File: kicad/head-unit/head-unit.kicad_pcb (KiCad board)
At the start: 4 copper layers, 59 parts, among them J1 Debug_Port, J2 Relay_Main_Power, J3 Steering_Wheel, J4 Power Port, J5 Car Connection, J6 Relay_Ign_Detect, J7 Pi, J8 DAC+, K1 Relay_Aux_Power, K2 Relay_Amplifier, SW1 SW_RST, U1 ADP1108AN-3.3, U2 STM32F401RCTx, U3 ADP1108AN-5

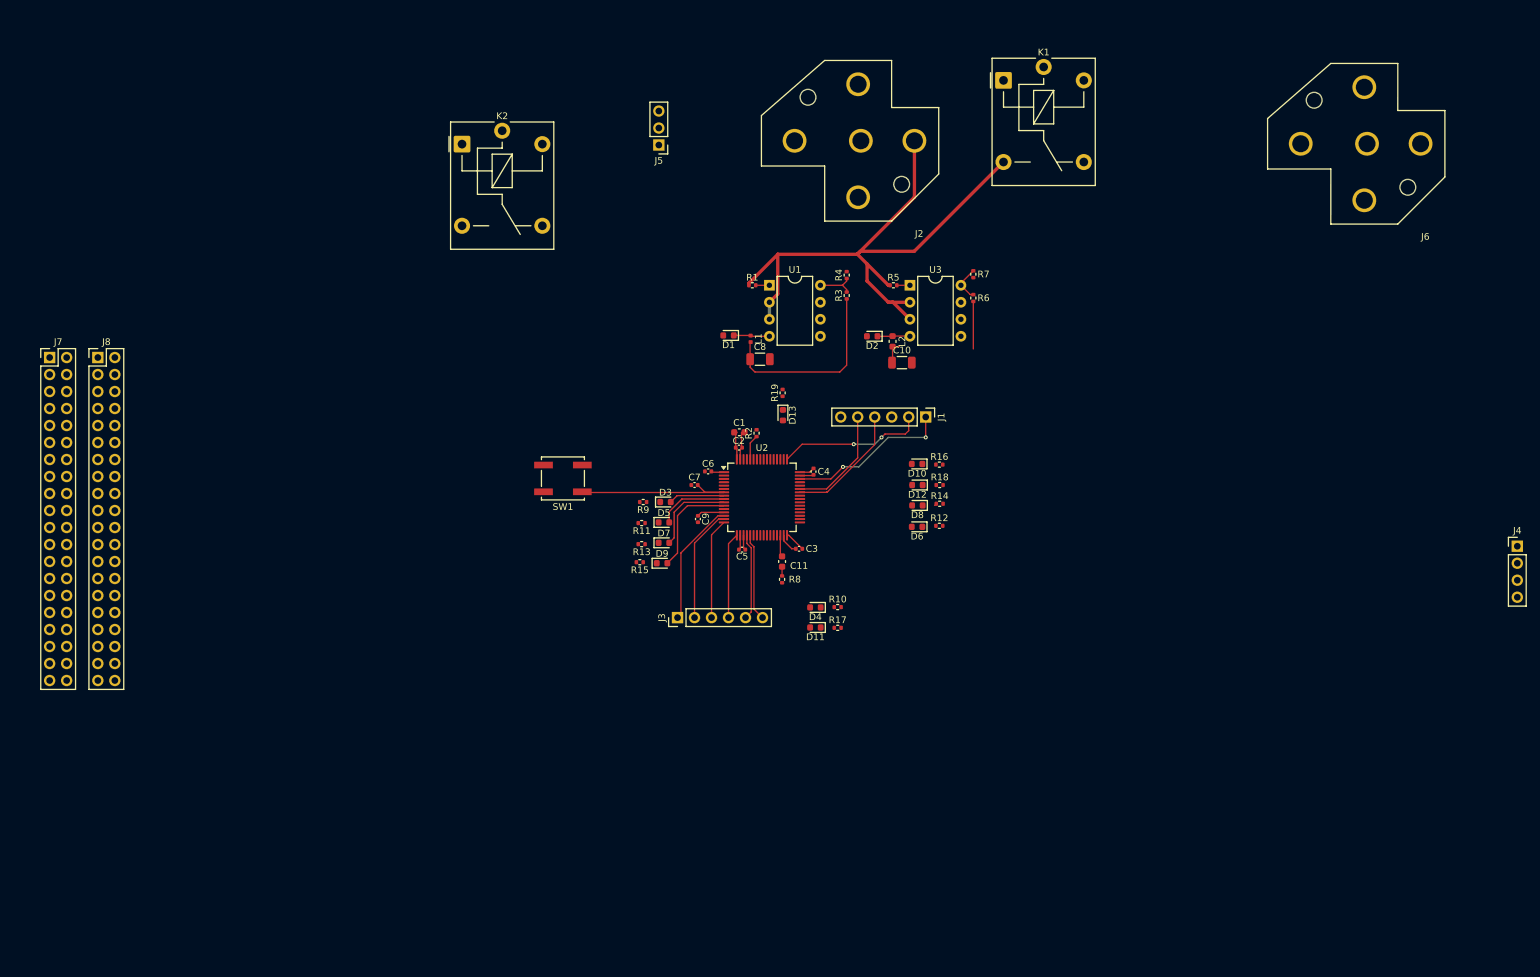
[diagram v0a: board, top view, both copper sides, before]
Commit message: Fix mosfets, switch to screw terminals and XT60
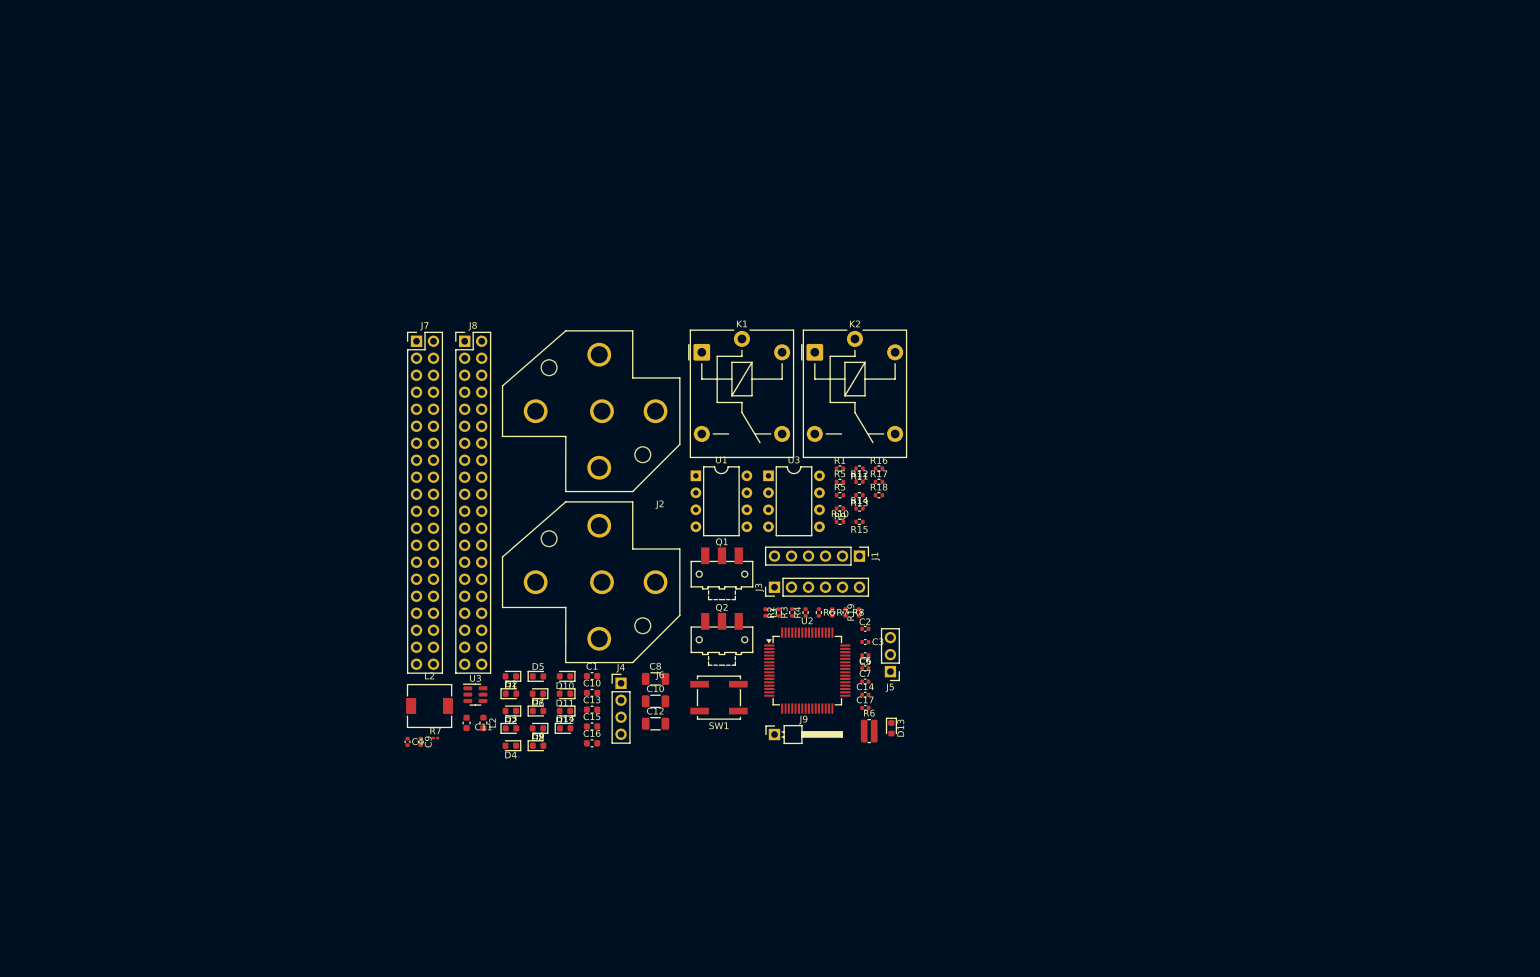
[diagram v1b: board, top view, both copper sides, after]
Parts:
- added C10: 10uF, Capacitor_SMD:C_0603_1608Metric, F.Cu at (133.5, 112.3)
- added C12: 100uF, Capacitor_SMD:C_1206_3216Metric, F.Cu at (143.0, 117.0)
- added C13: 22uF, Capacitor_SMD:C_0603_1608Metric, F.Cu at (133.5, 114.8)
- added C14: 100nF, Capacitor_SMD:C_0402_1005Metric, F.Cu at (174.4, 112.6)
- added C15: 22uF, Capacitor_SMD:C_0603_1608Metric, F.Cu at (133.5, 117.4)
- added C16: 10uF, Capacitor_SMD:C_0603_1608Metric, F.Cu at (133.5, 119.9)
- added C17: 100nF, Capacitor_SMD:C_0402_1005Metric, F.Cu at (174.4, 114.6)
- added D14: D_Schottky, Diode_SMD:D_0603_1608Metric, F.Cu at (129.5, 117.6)
- added D2: D_Schottky, Diode_SMD:D_0603_1608Metric, F.Cu at (121.4, 112.5)
- added J9: Amp_Remote, Connector_PinHeader_2.54mm:PinHeader_1x01_P2.54mm_Horizontal, F.Cu at (160.8, 118.6)
- added L2: 5.6uH, Inductor_SMD:L_6.3x6.3_H3, F.Cu at (109.3, 114.3)
- added Q1: NMOS, Button_Switch_SMD:SW_SPDT_CK-JS102011SAQN, F.Cu at (152.9, 94.6)
- added Q2: NMOS, Button_Switch_SMD:SW_SPDT_CK-JS102011SAQN, F.Cu at (152.9, 104.4)
- added R5: 10K, Resistor_SMD:R_0402_1005Metric, F.Cu at (170.6, 80.8)
- added R6: 102K2, Resistor_SMD:R_0612_1632Metric, F.Cu at (174.9, 118.0)
- added R7: 30R, Resistor_SMD:R_0201_0603Metric, F.Cu at (110.1, 119.1)
- added U3: TPS56339DDC, Package_TO_SOT_SMD:SOT-23-6, F.Cu at (116.1, 112.6)
- R3: value 456K -> 9K
- R4: value 33K -> 3K3
- moved J4 135.5 mm to (137.9, 110.9)
- moved J6 131.8 mm to (134.6, 95.8)
- moved J5 86.0 mm to (178.1, 109.2)
- moved L2 83.6 mm to (117.3, 116.8)
- moved D2 77.8 mm to (121.4, 115.0)
- moved C4 72.9 mm to (106.0, 119.7)
- moved D8 65.8 mm to (125.4, 117.6)
- moved C10 62.6 mm to (143.0, 113.6)
- moved D12 62.6 mm to (129.5, 115.0)
- moved D6 61.9 mm to (125.4, 112.5)
- moved D10 61.4 mm to (129.5, 109.9)
- moved K2 61.2 mm to (166.8, 61.5)
- moved K1 60.7 mm to (149.9, 61.5)
- moved D1 60.4 mm to (121.4, 109.9)
- moved J2 55.9 mm to (134.6, 70.3)
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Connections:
- J2 pad 87: Net-(U1-SW1) -> +12V_Switched
- K1 pad 14: Net-(U1-SW1) -> +12V_Switched
- K1 pad A1: GND -> Net-(Q1-S)
- K1 pad A2: Aux_Power -> +5V
- K2 pad 14: Amp_Remote -> Net-(J9-Pin_1)
- K2 pad A1: GND -> Net-(Q2-S)
- K2 pad A2: Amp_Remote_3V3 -> +5V
- R1 pad 1: Net-(U1-SW1) -> +12V_Switched
- U1 pad 2: Net-(U1-SW1) -> +12V_Switched
- U1 pad 3: Net-(U1-SW1) -> +12V_Switched
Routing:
- net Net-(U1-SW1): track 97.9 -> 0.00 mm
- net +3V3: track 40.7 -> 0.00 mm
- net Net-(U2-NRST): track 25.6 -> 0.00 mm
- net SWDIO: track 24.4 -> 0.00 mm, vias 2 -> 0
- net SWCLK: track 22.0 -> 0.00 mm, vias 2 -> 0
- net Steering_Yellow: track 18.6 -> 0.00 mm
- net USART_Debug_TX: track 18.2 -> 0.00 mm
- net Steering_Green: track 17.0 -> 0.00 mm
- net USART_Debug_RX: track 16.7 -> 0.00 mm
- net AA_TrackNext_LED: track 15.3 -> 0.00 mm
- net Steering_Blue: track 15.0 -> 0.00 mm
- net Steering_Brown: track 13.1 -> 0.00 mm
- net AA_VolDown_LED: track 12.9 -> 0.00 mm
- net Steering_Black: track 12.9 -> 0.00 mm
- net Steering_Red: track 12.8 -> 0.00 mm
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
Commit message: Add I2C, begin routing
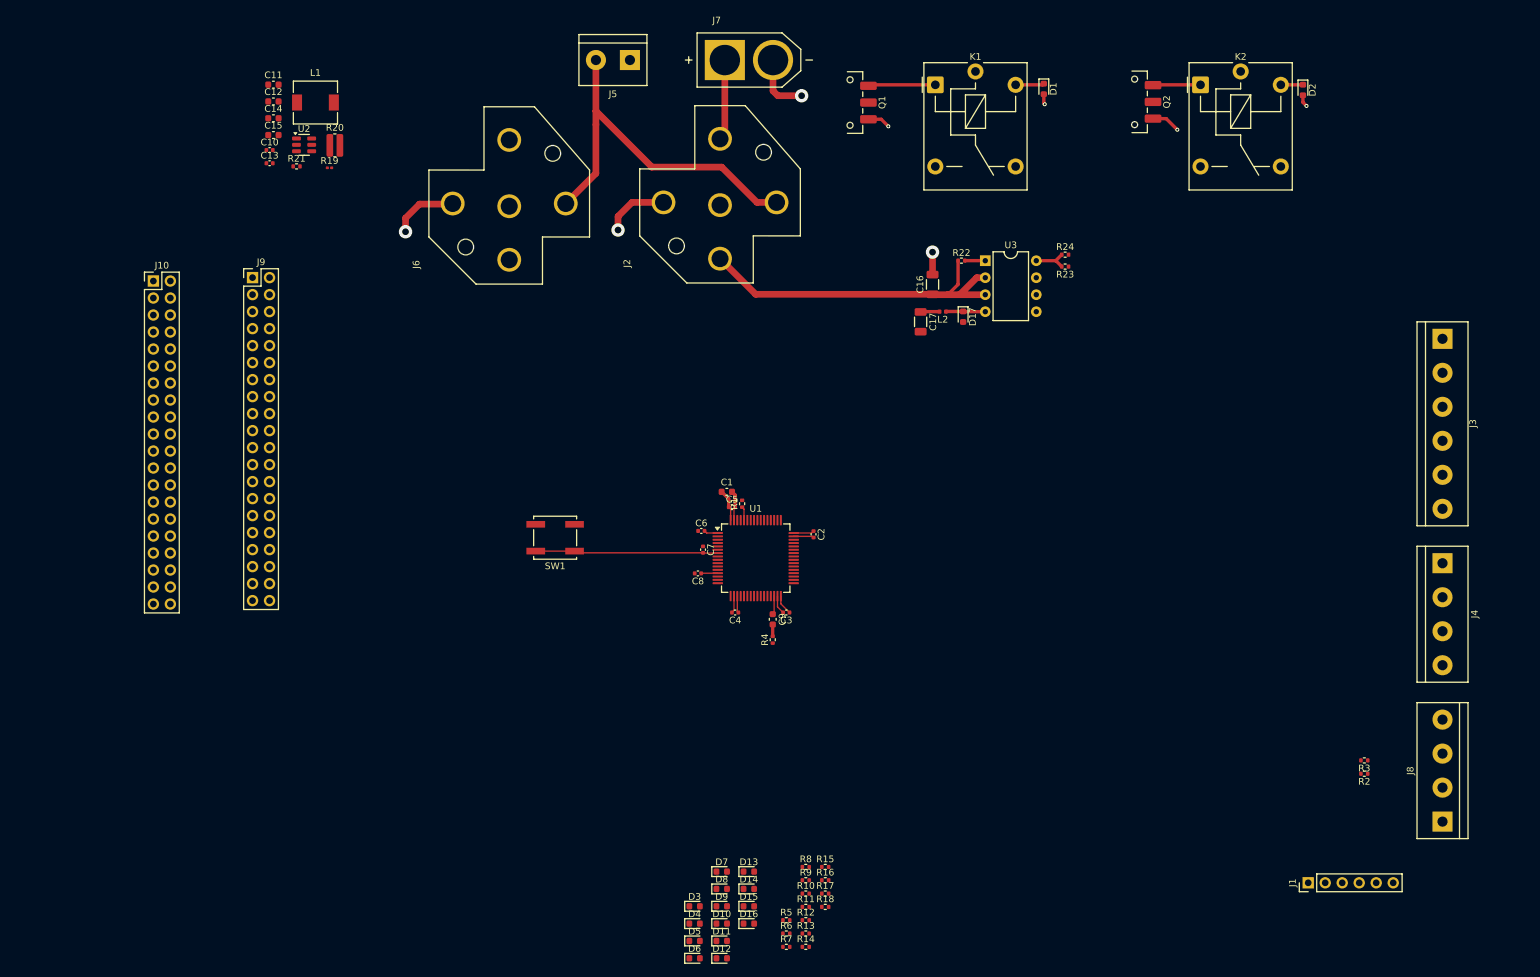
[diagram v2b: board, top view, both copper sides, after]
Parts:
- removed the C10 at (143.0, 113.6)
- removed the C10 at (133.5, 112.3)
- removed the D2 at (121.4, 115.0)
- removed the D2 at (121.4, 112.5)
- removed the L2 at (109.3, 114.3)
- removed the L2 at (117.3, 116.8)
- removed the R5 at (170.6, 82.8)
- removed the R5 at (170.6, 80.8)
- removed the R6 at (174.9, 118.0)
- removed the R6 at (167.4, 100.3)
- removed the R7 at (169.4, 100.3)
- removed the R7 at (110.1, 119.1)
- removed the U3 at (116.1, 112.6)
- removed the U3 at (159.9, 79.9)
- added C10: 100nF, Capacitor_SMD:C_0402_1005Metric, F.Cu at (85.4, 31.2)
- added D15: LED, LED_SMD:LED_0603_1608Metric, F.Cu at (157.0, 144.2)
- added D16: LED, LED_SMD:LED_0603_1608Metric, F.Cu at (157.0, 146.8)
- added D17: D_Schottky, Diode_SMD:D_0603_1608Metric, F.Cu at (189.0, 56.1)
- added D2: D_Schottky, Diode_SMD:D_0603_1608Metric, F.Cu at (239.7, 22.3)
- added J10: DAC+, Connector_PinHeader_2.54mm:PinHeader_2x20_P2.54mm_Vertical, F.Cu at (68.0, 50.8)
- added L2: 1uH, Inductor_SMD:L_0402_1005Metric, F.Cu at (185.9, 55.4)
- added R20: 102K2, Resistor_SMD:R_0612_1632Metric, F.Cu at (95.1, 30.5)
- added R21: 10K, Resistor_SMD:R_0402_1005Metric, F.Cu at (89.4, 33.7)
- added R22: 100R, Resistor_SMD:R_0402_1005Metric, F.Cu at (188.7, 47.8)
- added R23: 9K, Resistor_SMD:R_0402_1005Metric, F.Cu at (204.2, 48.6)
- added R24: 3K3, Resistor_SMD:R_0402_1005Metric, F.Cu at (204.2, 46.9)
- added R5: 2K2, Resistor_SMD:R_0402_1005Metric, F.Cu at (162.6, 146.3)
- added R6: 2K2, Resistor_SMD:R_0402_1005Metric, F.Cu at (162.6, 148.3)
- added R7: 2K2, Resistor_SMD:R_0402_1005Metric, F.Cu at (162.6, 150.3)
- added U3: ADP1108AN-3.3, Package_DIP:DIP-8_W7.62mm, F.Cu at (192.3, 47.8)
- C11: value 5uF -> 10uF
- C12: value 100uF -> 10uF; footprint Capacitor_SMD:C_1206_3216Metric -> Capacitor_SMD:C_0603_1608Metric
- C13: value 22uF -> 100nF; footprint Capacitor_SMD:C_0603_1608Metric -> Capacitor_SMD:C_0402_1005Metric
- C14: value 100nF -> 22uF; footprint Capacitor_SMD:C_0402_1005Metric -> Capacitor_SMD:C_0603_1608Metric
- C16: value 10uF -> 100uF; footprint Capacitor_SMD:C_0603_1608Metric -> Capacitor_SMD:C_1206_3216Metric
- C17: value 100nF -> 100uF; footprint Capacitor_SMD:C_0402_1005Metric -> Capacitor_SMD:C_1206_3216Metric
- C8: value 100uF -> 1 uF; footprint Capacitor_SMD:C_1206_3216Metric -> Capacitor_SMD:C_0402_1005Metric
- C9: value 1 uF -> 5uF; footprint Capacitor_SMD:C_0402_1005Metric -> Capacitor_SMD:C_0603_1608Metric
- D14: value D_Schottky -> LED; footprint Diode_SMD:D_0603_1608Metric -> LED_SMD:LED_0603_1608Metric
- J2, J6: footprint external_symbols:TE_VCF4-1000 -> vcf4:TE_VCF4-1000
- J3: footprint Connector_PinHeader_2.54mm:PinHeader_1x06_P2.54mm_Vertical -> TerminalBlock:TerminalBlock_bornier-6_P5.08mm
- J4: value Power Port -> Power_Port; footprint Connector_PinHeader_2.54mm:PinHeader_1x04_P2.54mm_Vertical -> TerminalBlock:TerminalBlock_bornier-4_P5.08mm
- J5: value Car Connection -> Remote; footprint Connector_PinHeader_2.54mm:PinHeader_1x03_P2.54mm_Vertical -> TerminalBlock:TerminalBlock_bornier-2_P5.08mm
- J7: value Pi -> XT60-M; footprint Connector_PinHeader_2.54mm:PinHeader_2x20_P2.54mm_Vertical -> xt60:AMASS_XT60-M
- J8: value DAC+ -> I2C_Interface; footprint Connector_PinHeader_2.54mm:PinHeader_2x20_P2.54mm_Vertical -> TerminalBlock:TerminalBlock_bornier-4_P5.08mm
- J9: value Amp_Remote -> Pi; footprint Connector_PinHeader_2.54mm:PinHeader_1x01_P2.54mm_Horizontal -> Connector_PinHeader_2.54mm:PinHeader_2x20_P2.54mm_Vertical
- L1: value 1uH -> 5.6uH; footprint Inductor_SMD:L_0402_1005Metric -> Inductor_SMD:L_6.3x6.3_H3
- Q1, Q2: footprint Button_Switch_SMD:SW_SPDT_CK-JS102011SAQN -> Button_Switch_SMD:SW_SPDT_CK_JS102011SAQN
- R1: value 100R -> 10K
- R19: value 2K2 -> 30R; footprint Resistor_SMD:R_0402_1005Metric -> Resistor_SMD:R_0201_0603Metric
- R2: value 10K -> 2K7
- R3: value 9K -> 2K7
- R4: value 3K3 -> 1R
- R8: value 1R -> 2K2
- U1: value ADP1108AN-3.3 -> STM32F401RCTx; footprint Package_DIP:DIP-8_W7.62mm -> Package_QFP:LQFP-64_10x10mm_P0.5mm
- U2: value STM32F401RCTx -> TPS56339DDC; footprint Package_QFP:LQFP-64_10x10mm_P0.5mm -> Package_TO_SOT_SMD:SOT-23-6
- moved J8 162.8 mm to (260.6, 131.6), turned to 90 degrees
- moved J4 124.0 mm to (260.6, 93.0), turned to -90 degrees
- moved C14 123.5 mm to (85.9, 26.5)
- moved D1 118.5 mm to (201.0, 22.1), turned to -90 degrees
- moved C12 109.1 mm to (85.9, 24.0)
- moved U2 108.7 mm to (90.5, 30.5)
- moved J3 106.5 mm to (260.6, 59.4), turned to -90 degrees
- moved J9 103.6 mm to (82.8, 50.3)
- moved R19 103.3 mm to (94.3, 33.9), turned to 0 degrees
- moved L1 101.6 mm to (92.2, 24.1), turned to 0 degrees
- moved Q2 101.3 mm to (214.6, 24.0), turned to -90 degrees
- moved C15 100.4 mm to (85.9, 29.0)
- moved C11 99.6 mm to (85.9, 21.5), turned to 0 degrees
- moved J5 99.3 mm to (139.2, 17.8)
- moved C13 94.8 mm to (85.4, 33.2)
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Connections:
- C11 pad 1: Net-(U2-VCAP1) -> +12V_Switched
- C11 pad 2: Net-(C11-Pad2) -> GND
- C13 pad 1: +5V -> +12V_Switched
- C14 pad 1: Net-(C14-Pad1) -> +5V
- C14 pad 2: Net-(U3-SW) -> GND
- C17 pad 1: +12V_Switched -> +3V3
- C6 pad 2: Net-(U2-VBAT) -> Net-(U1-VBAT)
- C7 pad 2: Net-(U2-NRST) -> Net-(U1-NRST)
- C8 pad 1: +3V3 -> Net-(U1-VREF+)
- C8 pad 2: GND -> +3V3
- C9 pad 1: Net-(U2-VREF+) -> Net-(U1-VCAP1)
- C9 pad 2: +3V3 -> Net-(C9-Pad2)
- D1 pad 1: Net-(D1-K) -> +5V
- D14 pad 1: +5V -> Net-(D14-K)
- D14 pad 2: GND -> Power_LED
- J4 pad 1: GND -> +3V3
- J4 pad 2: +3V3 -> +5V
- J4 pad 3: +5V -> +12V
- J4 pad 4: +12V -> GND
- J5 pad 1: +12V -> Amp_Remote
- J5 pad 2: GND -> Car_Remote
- J8 pad 1: Pi_3V3 -> +3V3
- J8 pad 2: +5V -> Net-(J8-Pin_2)
- J8 pad 3: DAC_I2C_SDA -> Net-(J8-Pin_3)
- J8 pad 4: +5V -> GND
- J9 pad 1: Net-(J9-Pin_1) -> Pi_3V3
- K1 pad A1: Net-(Q1-S) -> Net-(Q1-D)
- K2 pad 14: Net-(J9-Pin_1) -> Amp_Remote
- K2 pad A1: Net-(Q2-S) -> Net-(Q2-D)
- L1 pad 1: Net-(D1-K) -> Net-(U2-SW)
- L1 pad 2: +3V3 -> +5V
- Q1 pad 1: GND -> Net-(Q1-D)
- Q1 pad 3: Net-(Q1-S) -> GND
- Q2 pad 1: GND -> Net-(Q2-D)
- Q2 pad 3: Net-(Q2-S) -> GND
- R1 pad 1: +12V_Switched -> Net-(U1-BOOT0)
- R1 pad 2: Net-(U1-Ilim) -> GND
- R10 pad 1: Net-(D4-K) -> Net-(D8-K)
- R11 pad 1: Net-(D5-K) -> Net-(D9-K)
- R12 pad 1: Net-(D6-K) -> Net-(D10-K)
- R13 pad 1: Net-(D7-K) -> Net-(D11-K)
- R14 pad 1: Net-(D8-K) -> Net-(D12-K)
- R15 pad 1: Net-(D9-K) -> Net-(D13-K)
- R16 pad 1: Net-(D10-K) -> Net-(D14-K)
- R17 pad 1: Net-(D11-K) -> Net-(D15-K)
- R18 pad 1: Net-(D12-K) -> Net-(D16-K)
- R19 pad 1: Net-(D13-K) -> Net-(U2-BOOT)
- R19 pad 2: GND -> Net-(C10-Pad1)
- R2 pad 1: Net-(U2-BOOT0) -> +3V3
- R2 pad 2: GND -> Net-(J8-Pin_3)
- R3 pad 2: Net-(U1-SENSE) -> Net-(J8-Pin_2)
- R4 pad 1: Net-(U1-SENSE) -> GND
- R4 pad 2: GND -> Net-(C9-Pad2)
- R8 pad 1: GND -> Net-(D6-K)
- R8 pad 2: Net-(C11-Pad2) -> GND
- R9 pad 1: Net-(D3-K) -> Net-(D7-K)
- SW1 pad 2: Net-(U2-NRST) -> Net-(U1-NRST)
- U1 pad 1: Net-(U1-Ilim) -> Net-(U1-VBAT)
- U1 pad 2: +12V_Switched -> AA_BrightnessDown_LED
- U1 pad 3: +12V_Switched -> unconnected-(U1-PC14-Pad3)
- U1 pad 4: Net-(D1-K) -> unconnected-(U1-PC15-Pad4)
- U1 pad 5: GND -> unconnected-(U1-PH0-Pad5)
- U1 pad 7: unconnected-(U1-SET-Pad7) -> Net-(U1-NRST)
- U1 pad 8: Net-(U1-SENSE) -> AA_Mute_LED
- U2 pad 1: Net-(U2-VBAT) -> GND
- U2 pad 2: unconnected-(U2-PC13-Pad2) -> Net-(U2-SW)
- U2 pad 3: unconnected-(U2-PC14-Pad3) -> +12V_Switched
- U2 pad 4: unconnected-(U2-PC15-Pad4) -> Net-(U2-FB)
- U2 pad 5: unconnected-(U2-PH0-Pad5) -> +12V_Switched
- U2 pad 6: unconnected-(U2-PH1-Pad6) -> Net-(U2-BOOT)
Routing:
- net Car_Remote: track 0.00 -> 56.0 mm
- net GND: track 0.00 -> 55.9 mm, vias 0 -> 8
- net +12V_Switched: track 0.00 -> 52.5 mm
- net Net-(U1-NRST): track 0.00 -> 27.3 mm
- net +3V3: track 0.00 -> 16.2 mm
- net +12V: track 0.00 -> 12.1 mm
- net Net-(Q1-D): track 0.00 -> 10.1 mm
- net +5V: track 0.00 -> 7.60 mm
- net Net-(Q2-D): track 0.00 -> 7.11 mm
- net Net-(D17-K): track 0.00 -> 5.90 mm
- net Net-(U3-SENSE): track 0.00 -> 5.44 mm
- net Net-(U3-Ilim): track 0.00 -> 3.06 mm
- net Net-(U1-VCAP1): track 0.00 -> 2.78 mm
- net Net-(U1-VREF+): track 0.00 -> 2.50 mm
- net Net-(U1-VBAT): track 0.00 -> 2.10 mm
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
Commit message: WIP routing
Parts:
- moved J3 146.4 mm to (123.2, 109.9), turned to 0 degrees
- moved J8 97.9 mm to (165.1, 109.9), turned to 0 degrees
- moved J1 86.2 mm to (184.8, 74.9)
- moved R3 80.4 mm to (170.7, 103.9)
- moved R2 76.0 mm to (175.8, 103.9)
- moved R17 66.8 mm to (158.8, 76.2), turned to 90 degrees
- moved D12 65.8 mm to (173.4, 89.4), turned to 180 degrees
- moved D15 64.9 mm to (158.8, 79.4), turned to -90 degrees
- moved R16 64.5 mm to (161.5, 76.2), turned to 90 degrees
- moved D14 62.4 mm to (161.5, 79.4), turned to -90 degrees
- moved R15 62.3 mm to (164.1, 76.2), turned to 90 degrees
- moved R14 61.9 mm to (176.5, 89.4)
- moved R18 60.8 mm to (143.3, 88.9), turned to 180 degrees
- moved D13 60.1 mm to (164.1, 79.4), turned to -90 degrees
- moved D6 60.1 mm to (173.4, 97.2), turned to 180 degrees
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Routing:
- net GND: track 55.9 -> 113.7 mm, vias 8 -> 32
- net Net-(J8-Pin_3): track 0.00 -> 43.2 mm
- net Steering_Yellow: track 0.00 -> 35.3 mm
- net Steering_Green: track 0.00 -> 30.0 mm
- net Net-(J8-Pin_2): track 0.00 -> 28.7 mm
- net Steering_Blue: track 0.00 -> 24.7 mm
- net Steering_Red: track 0.00 -> 20.8 mm
- net Steering_Black: track 0.00 -> 19.2 mm
- net Steering_Brown: track 0.00 -> 15.1 mm
- net AA_TrackNext_LED: track 0.00 -> 13.7 mm
- net AA_VolDown_LED: track 0.00 -> 12.6 mm
- net +3V3: track 16.2 -> 27.8 mm, vias 0 -> 5
- net AA_VolUp_LED: track 0.00 -> 10.9 mm
- net Aux_Power_LED: track 0.00 -> 10.4 mm
- net Net-(U2-FB): track 0.00 -> 10.3 mm
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
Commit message: More routing
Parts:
- moved D2 76.4 mm to (179.4, 31.6)
- moved K2 76.4 mm to (164.1, 30.8)
- moved Q2 76.4 mm to (154.2, 33.3)
- moved D17 74.8 mm to (131.3, 78.7)
- moved L2 74.8 mm to (128.3, 78.0)
- moved R24 74.8 mm to (146.6, 69.4)
- moved C16 74.8 mm to (126.8, 73.9)
- moved C17 74.8 mm to (125.0, 79.5)
- moved R22 74.8 mm to (131.1, 70.3)
- moved R23 74.8 mm to (146.6, 71.2)
- moved U3 74.8 mm to (134.7, 70.3)
- moved J6 58.7 mm to (195.5, 54.5)
- moved J7 47.0 mm to (126.0, 29.0)
- moved D1 44.4 mm to (180.0, 55.8)
- moved K1 44.0 mm to (164.1, 54.8)
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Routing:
- net +12V: track 12.1 -> 143.9 mm
- net Car_Remote: track 56.0 -> 109.6 mm, vias 0 -> 2
- net +12V_Switched: track 60.0 -> 102.3 mm
- net Amp_Remote: track 0.00 -> 27.8 mm
- net +3V3: track 27.8 -> 46.5 mm, vias 5 -> 7
- net Net-(Q1-D): track 10.1 -> 0.00 mm
- net GND: track 113.7 -> 121.1 mm, vias 32 -> 33

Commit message: Fix pi moutning holes?
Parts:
- added REF**: MountingHole_2.5mm_Pad, MountingHole:MountingHole_2.5mm_Pad, F.Cu at (112.0, 120.5)
- added REF**: MountingHole_2.5mm_Pad, MountingHole:MountingHole_2.5mm_Pad, F.Cu at (63.0, 120.5)
- added REF**: MountingHole_2.5mm_Pad, MountingHole:MountingHole_2.5mm_Pad, F.Cu at (63.0, 62.5)
- added REF**: MountingHole_2.5mm_Pad, MountingHole:MountingHole_2.5mm_Pad, F.Cu at (112.0, 62.5)
- moved J9 1.11 mm to (111.0, 67.4)
- moved C2 0.65 mm to (166.6, 88.0)
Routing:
- net SWDIO: track 0.00 -> 45.4 mm, vias 0 -> 2
- net SWCLK: track 0.00 -> 43.1 mm
- net USART_Debug_TX: track 0.00 -> 27.9 mm
- net USART_Debug_RX: track 0.00 -> 27.4 mm
- net GND: track 121.1 -> 126.0 mm, vias 33 -> 34
- net +3V3: track 46.5 -> 50.9 mm, vias 7 -> 8

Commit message: Stuff
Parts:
- Q2: footprint Button_Switch_SMD:SW_SPDT_CK_JS102011SAQN -> Button_Switch_SMD:SW_SPDT_CK-JS102011SAQN
- R1, R21: footprint Resistor_SMD:R_0402_1005Metric -> Resistor_SMD:R_0603_1608Metric
- R20: footprint Resistor_SMD:R_0612_1632Metric -> Resistor_SMD:R_0805_2012Metric
